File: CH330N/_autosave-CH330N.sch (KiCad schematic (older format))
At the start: 20 parts, among them J2 Conn_01x06, P1 USB_C_Plug_USB2.0, U1 CH330N, U2 AP2127K-3.3

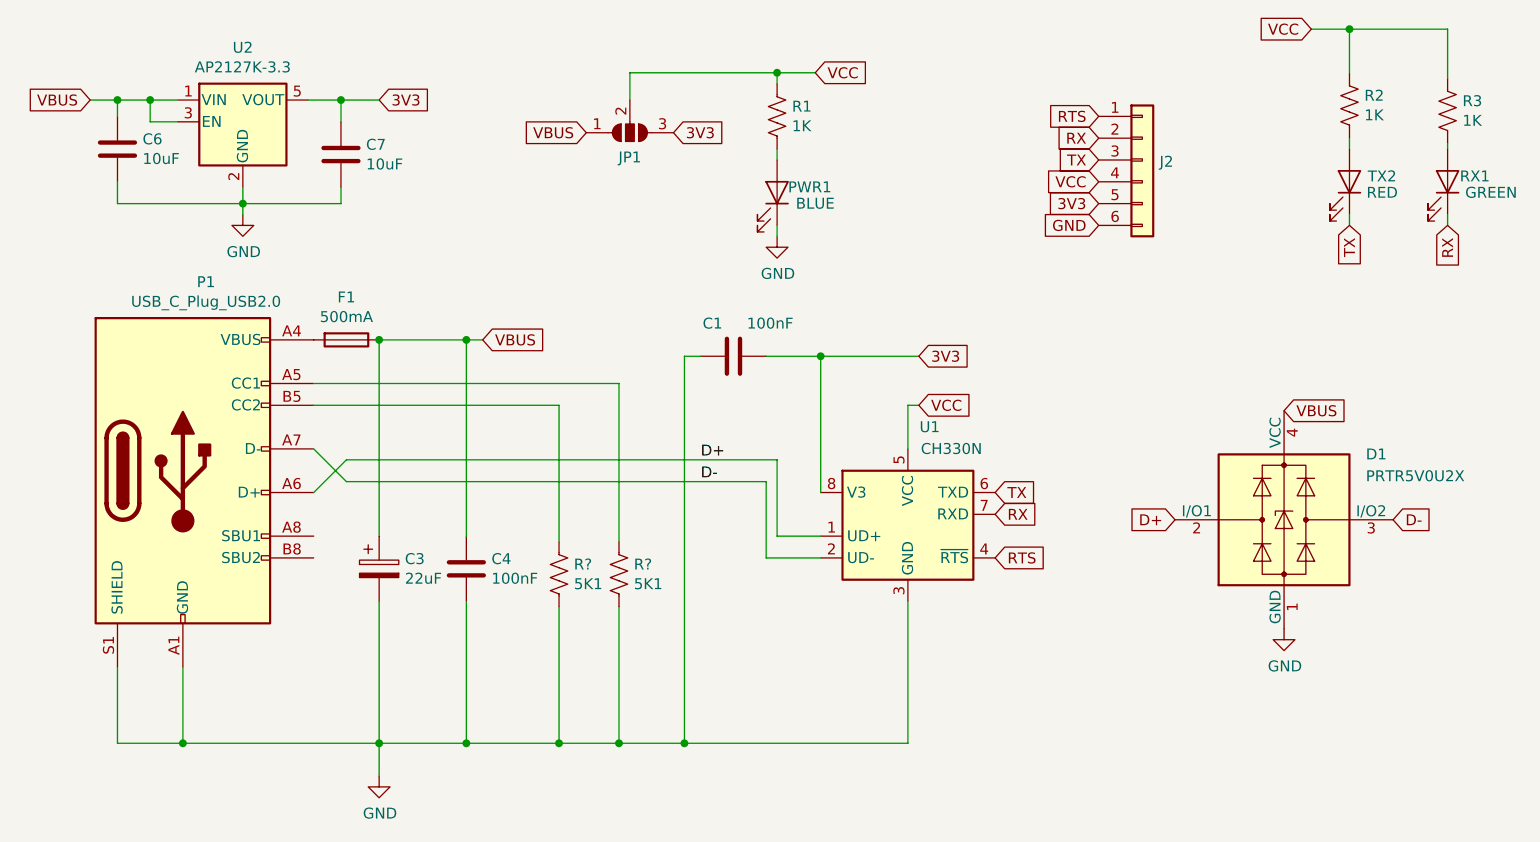
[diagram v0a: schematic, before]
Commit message: SirUSB Updates
CH330N Revision 1.1 + 3D Render Improvement
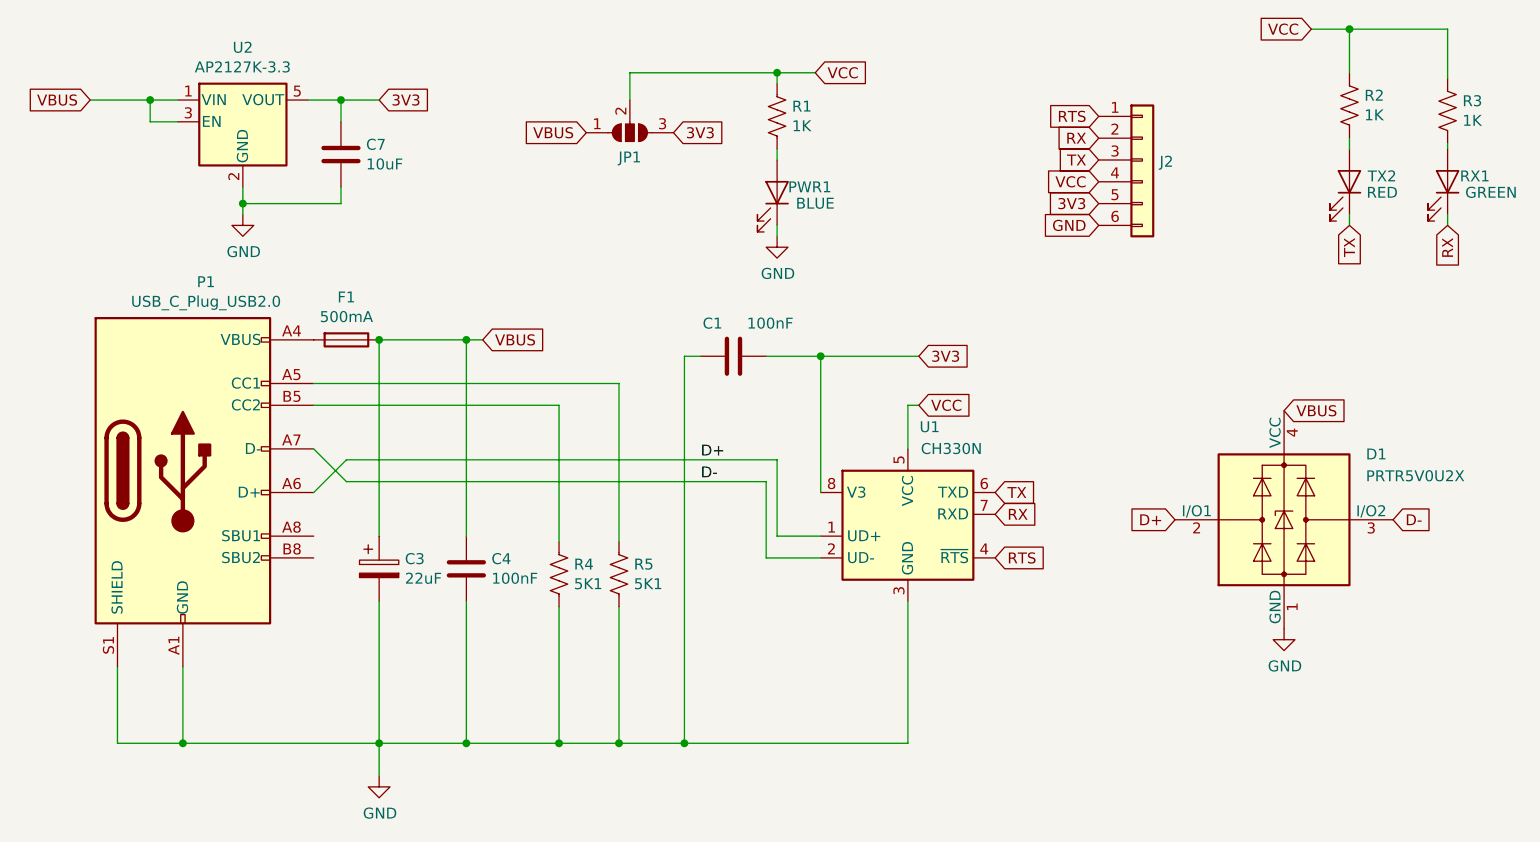
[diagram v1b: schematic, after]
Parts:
- removed C6: 10uF, Capacitor_SMD:C_0805_2012Metric, symbol Device:C
- gave numbers to parts that had none: 2
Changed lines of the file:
@@
 VBUS
-Wire Wire Line
-	1025 950  1150 950
 Wire Wire Line
 	1300 950  1300 1050
@@
 Text GLabel 5650 1525 0    50   Input ~ 0
 GND
-$Comp
-L Device:C C6
-U 1 1 5E4982E1
-P 1150 1175
-F 0 "C6" H 1265 1220 50  0000 L CNN
-F 1 "10uF" H 1265 1130 50  0000 L CNN
-F 2 "Capacitor_SMD:C_0805_2012Metric" H 1188 1025 50  0001 C CNN
-F 3 "~" H 1150 1175 50  0001 C CNN
-F 4 "C95841" H 1150 1175 50  0001 C CNN "Part"
-	1    1150 1175
-	1    0    0    -1
-$EndComp
 Wire Wire Line
 	2175 1050 2175 950
@@
 Wire Wire Line
 	2175 950  2350 950
-Wire Wire Line
-	1150 950  1150 1025
-Connection ~ 1150 950
-Wire Wire Line
-	1150 950  1300 950
-Wire Wire Line
-	1150 1325 1150 1425
-Wire Wire Line
-	1150 1425 1725 1425
 Connection ~ 1725 1425
 Wire Wire Line
@@
 	6800 625  7250 625
 $Comp
-L Device:R_US R?
+L Device:R_US R4
 U 1 1 5E9C0593
 P 3175 3125
-F 0 "R?" H 3243 3170 50  0000 L CNN
+F 0 "R4" H 3243 3170 50  0000 L CNN
 F 1 "5K1" H 3243 3080 50  0000 L CNN
 F 2 "Resistor_SMD:R_0603_1608Metric" V 3215 3115 50  0001 C CNN
@@
 $EndComp
 $Comp
-L Device:R_US R?
+L Device:R_US R5
 U 1 1 5E9C1822
 P 3450 3125
-F 0 "R?" H 3518 3170 50  0000 L CNN
+F 0 "R5" H 3518 3170 50  0000 L CNN
 F 1 "5K1" H 3518 3080 50  0000 L CNN
 F 2 "Resistor_SMD:R_0603_1608Metric" V 3490 3115 50  0001 C CNN
@@
 Wire Wire Line
 	3450 3900 3750 3900
+Wire Wire Line
+	1025 950  1300 950
 $EndSCHEMATC
